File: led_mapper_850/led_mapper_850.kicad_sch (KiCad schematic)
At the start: 555 parts, among them J1 Conn_02x12_Top_Bottom

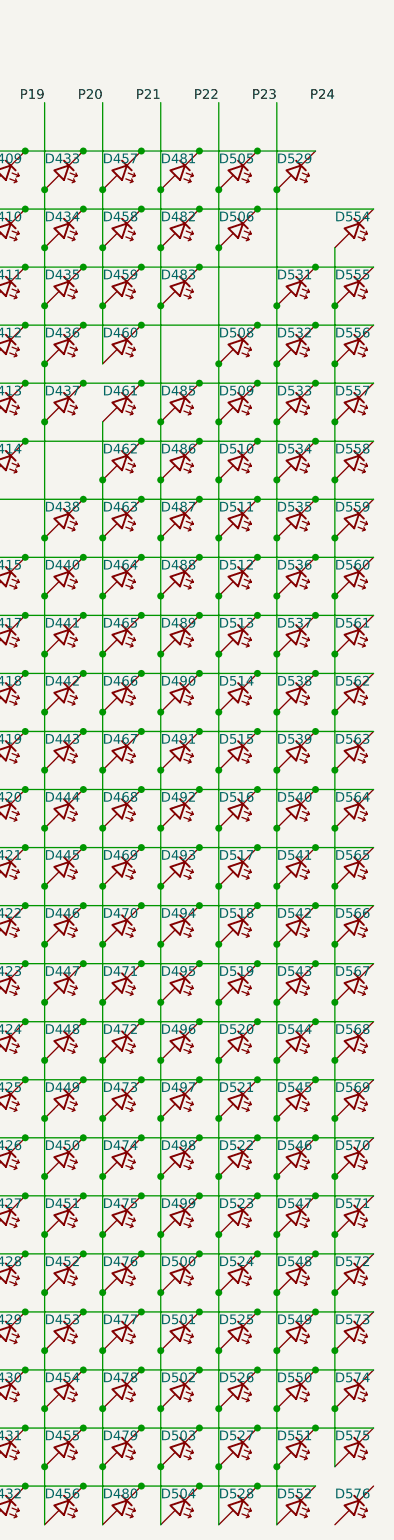
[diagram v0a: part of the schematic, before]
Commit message: run ERC & fix connections
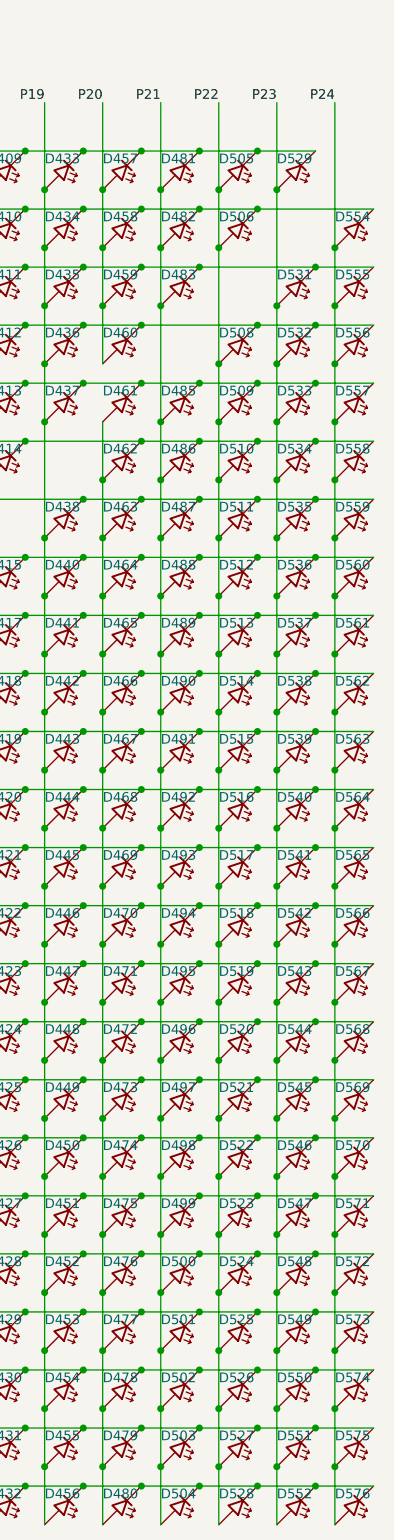
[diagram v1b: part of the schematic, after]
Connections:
- net P01: now also D576.1 (K)
- net P24: now also D554.2 (A), D555.2 (A), D556.2 (A), D557.2 (A), D558.2 (A), D559.2 (A), D560.2 (A), D561.2 (A), D562.2 (A), D563.2 (A), D564.2 (A), D565.2 (A), D566.2 (A), D567.2 (A), D568.2 (A), D569.2 (A), D570.2 (A), D571.2 (A), D572.2 (A), D573.2 (A), D574.2 (A), D575.2 (A), D576.2 (A)
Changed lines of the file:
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@@
 	)
 	(junction
+		(at 392.43 66.04)
+		(diameter 0)
+		(color 0 0 0 0)
+	)
+	(junction
 		(at 306.07 53.34)
 		(diameter 0)
@@
 	)
 	(junction
+		(at 389.89 228.6)
+		(diameter 0)
+		(color 0 0 0 0)
+	)
+	(junction
 		(at 369.57 119.38)
 		(diameter 0)
@@
 	)
 	(junction
+		(at 392.43 226.06)
+		(diameter 0)
+		(color 0 0 0 0)
+	)
+	(junction
 		(at 367.03 220.98)
 		(diameter 0)
@@
 	(wire
 		(pts
+			(xy 392.43 46.99) (xy 392.43 66.04)
+		)
+		(stroke
+			(width 0)
+			(type default)
+		)
+	)
+	(wire
+		(pts
 			(xy 260.35 106.68) (xy 267.97 106.68)
 		)
@@
 	(wire
 		(pts
+			(xy 392.43 226.06) (xy 392.43 233.68)
+		)
+		(stroke
+			(width 0)
+			(type default)
+		)
+	)
+	(wire
+		(pts
 			(xy 255.27 104.14) (xy 255.27 111.76)
 		)
@@
 		)
 		(stroke
+			(width 0)
+			(type default)
+		)
+	)
+	(wire
+		(pts
+			(xy 389.89 228.6) (xy 397.51 228.6)
+		)
+		(stroke

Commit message: associate footprints
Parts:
- D1, D10, D100, D101, D102, D103, D104, D105, D106, D107, D108, D109, D11, D110, D111, D112, D113, D114, D115, D116, D117, D118, D12, D120, D121, D122, D123, D124, D125, D126, D127, D128, D129, D13, D130, D131, D132, D133, D134, D135, D136, D137, D138, D139, D14, D140, D141, D142, D144, D145, D146, D147, D148, D149, D15, D150, D151, D152, D153, D154, D155, D156, D157, D158, D159, D16, D160, D161, D162, D163, D164, D165, D167, D168, D169, D17, D170, D171, D172, D173, D174, D175, D176, D177, D178, D179, D18, D180, D181, D182, D183, D184, D185, D186, D187, D189, D19, D190, D191, D192, D193, D194, D195, D196, D197, D198, D199, D2, D20, D200, D201, D202, D203, D204, D205, D206, D207, D208, D209, D21, D211, D212, D213, D214, D215, D216, D217, D218, D219, D22, D220, D221, D222, D223, D224, D225, D226, D227, D228, D229, D23, D230, D231, D232, D234, D235, D236, D237, D238, D239, D24, D240, D241, D242, D243, D244, D245, D246, D247, D248, D249, D25, D250, D251, D252, D253, D254, D255, D256, D258, D259, D26, D260, D261, D262, D263, D264, D265, D266, D267, D268, D269, D270, D271, D272, D273, D274, D275, D276, D277, D278, D279, D28, D280, D282, D283, D284, D285, D286, D287, D288, D289, D29, D290, D291, D292, D293, D294, D295, D296, D297, D298, D299, D3, D30, D300, D301, D302, D303, D305, D306, D307, D308, D309, D31, D310, D311, D312, D313, D314, D315, D316, D317, D318, D319, D32, D320, D321, D322, D323, D324, D325, D326, D328, D329, D33, D330, D331, D332, D333, D334, D335, D336, D337, D338, D339, D34, D340, D341, D342, D343, D344, D345, D346, D347, D348, D35, D350, D351, D352, D353, D354, D355, D356, D357, D358, D359, D36, D360, D361, D362, D363, D364, D365, D366, D367, D368, D369, D37, D370, D371, D373, D374, D375, D376, D377, D378, D379, D38, D380, D381, D382, D383, D384, D385, D386, D387, D388, D389, D39, D390, D391, D392, D393, D394, D395, D396, D397, D398, D399, D4, D40, D400, D401, D402, D403, D404, D405, D406, D407, D408, D409, D41, D410, D411, D412, D413, D414, D415, D417, D418, D419, D42, D420, D421, D422, D423, D424, D425, D426, D427, D428, D429, D43, D430, D431, D432, D433, D434, D435, D436, D437, D438, D44, D440, D441, D442, D443, D444, D445, D446, D447, D448, D449, D45, D450, D451, D452, D453, D454, D455, D456, D457, D458, D459, D46, D460, D461, D462, D463, D464, D465, D466, D467, D468, D469, D47, D470, D471, D472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: footprint (none) -> LED_SMD:LED_0201_0603Metric
- J1: footprint (none) -> ccatlib:PinSocket_2x12_P2.54mm_Vertical_SMD_custom
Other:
- moved on the sheet: D1, D10, D100, D101, D102, D103, D104, D105, D106, D107, D108, D109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

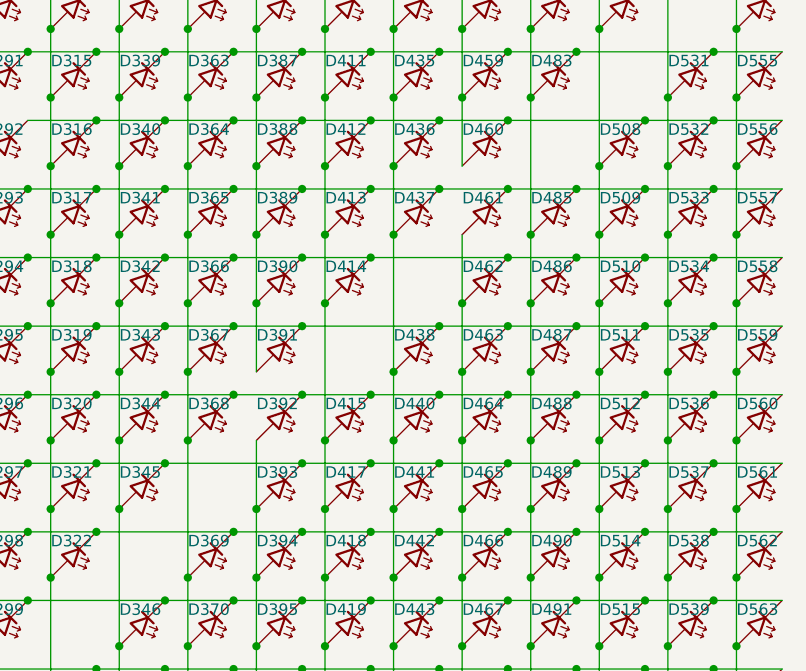
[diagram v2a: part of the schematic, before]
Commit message: fix mistakes on diagonal
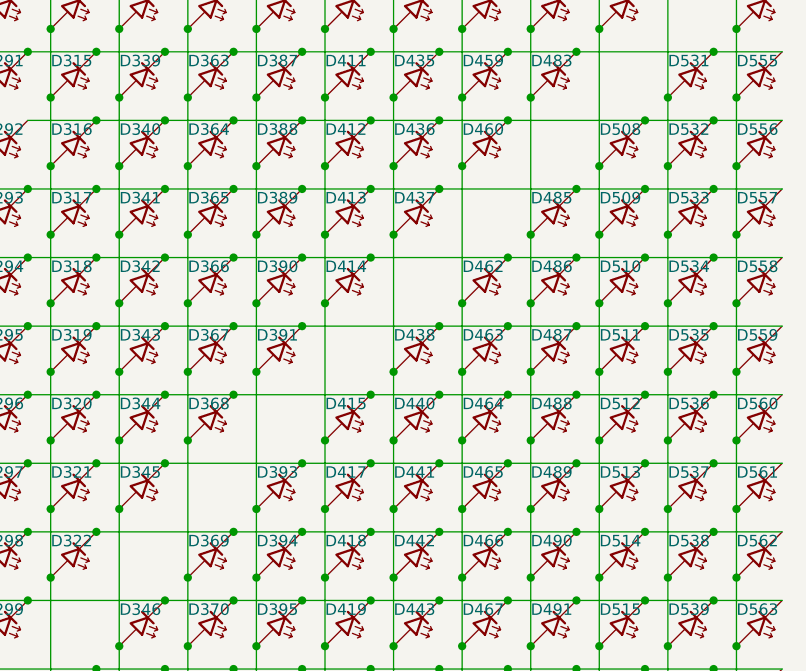
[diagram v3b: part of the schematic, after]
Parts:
- removed D392, D461: LED, LED_SMD:LED_0201_0603Metric, symbol Device:LED_45deg
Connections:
- net P17: now also D393.2 (A), D394.2 (A), D395.2 (A), D396.2 (A), D397.2 (A), D398.2 (A), D399.2 (A), D400.2 (A), D401.2 (A), D402.2 (A), D403.2 (A), D404.2 (A), D405.2 (A), D406.2 (A), D407.2 (A), D408.2 (A)
- net P20: now also D462.2 (A), D463.2 (A), D464.2 (A), D465.2 (A), D466.2 (A), D467.2 (A), D468.2 (A), D469.2 (A), D470.2 (A), D471.2 (A), D472.2 (A), D473.2 (A), D474.2 (A), D475.2 (A), D476.2 (A), D477.2 (A), D478.2 (A), D479.2 (A), D480.2 (A)
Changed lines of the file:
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@@
 	)
 	(junction
+		(at 289.56 76.2)
+		(diameter 0)
+		(color 0 0 0 0)
+	)
+	(junction
 		(at 320.04 175.26)
 		(diameter 0)
@@
 	)
 	(junction
-		(at 294.64 78.74)
-		(diameter 0)
-		(color 0 0 0 0)
-	)
-	(junction
 		(at 228.6 205.74)
 		(diameter 0)
@@
 	)
 	(junction
-		(at 271.78 101.6)
-		(diameter 0)
-		(color 0 0 0 0)
-	)
-	(junction
 		(at 213.36 106.68)
 		(diameter 0)
@@
 	)
 	(junction
+		(at 266.7 99.06)
+		(diameter 0)
+		(color 0 0 0 0)
+	)
+	(junction
 		(at 195.58 193.04)
 		(diameter 0)
@@
 	(wire
 		(pts
-			(xy 294.64 78.74) (xy 302.26 78.74)
+			(xy 287.02 78.74) (xy 302.26 78.74)
 		)
 		(stroke
@@
 	(wire
 		(pts
-			(xy 266.7 106.68) (xy 266.7 114.3)
+			(xy 266.7 99.06) (xy 266.7 114.3)
 		)
 		(stroke
@@
 	(wire
 		(pts
-			(xy 271.78 101.6) (xy 279.4 101.6)
-		)
-		(stroke
-			(width 0)
-			(type default)
-		)
-	)
-	(wire
-		(pts
 			(xy 281.94 99.06) (xy 281.94 106.68)
 		)
@@
 	(wire
 		(pts
-			(xy 264.16 101.6) (xy 271.78 101.6)
+			(xy 264.16 101.6) (xy 279.4 101.6)
 		)
 		(stroke
@@
 	(wire
 		(pts
-			(xy 287.02 78.74) (xy 294.64 78.74)
-		)
-		(stroke
-			(width 0)
-			(type default)
-		)
-	)
-	(wire
-		(pts
 			(xy 256.54 63.5) (xy 264.16 63.5)
 		)
@@
 	(wire
 		(pts
-			(xy 289.56 83.82) (xy 289.56 91.44)
+			(xy 289.56 76.2) (xy 289.56 91.44)
 		)
 		(stroke
@@
 	(symbol
 		(lib_id "Device:LED_45deg")
-		(at 292.1 81.28 90)
-		(unit 1)
-		(exclude_from_sim no)
-		(in_bom yes)
-		(on_board yes)
-		(dnp no)
-		(property "Reference" "D461"
-			(at 289.56 79.756 90)
-			(effects
-				(font
-					(size 1.27 1.27)
-				)
-				(justify right)
-			)
-		)
-		(property "Value" "LED"
-			(at 292.608 83.058 90)
-			(effects
-				(font
-					(size 1.27 1.27)
-				)
-				(justify right)
-				(hide yes)
-			)
-		)
-		(property "Footprint" "LED_SMD:LED_0201_0603Metric"
-			(at 292.1 81.28 0)
-			(effects
-				(font
-					(size 1.27 1.27)
-				)
-				(hide yes)
-			)
-		)
-		(property "Datasheet" "~"
-			(at 292.1 81.28 0)
-			(effects
-				(font
-					(size 1.27 1.27)
-				)
-				(hide yes)
-			)
-		)
-		(property "Description" "Light emitting diode, rotated by 45°"
-			(at 292.1 81.28 0)
-			(effects
-				(font
-					(size 1.27 1.27)
-				)
-				(hide yes)
-			)
-		)
-		(pin "1"
-		)
-		(pin "2"
-		)
-		(instances
-			(project "led_mapper_850"
-				(path "/51b7e780-688f-494d-9172-4437a593740a"
-					(reference "D461")
-					(unit 1)
-				)
-			)
-		)
-	)
-	(symbol
-		(lib_id "Device:LED_45deg")
 		(at 215.9 165.1 90)
 		(unit 1)
@@
 					(unit 1)
 				)
-			)
-		)
-	)
-	(symbol
-		(lib_id "Device:LED_45deg")
-		(at 269.24 104.14 90)
-		(unit 1)
-		(exclude_from_sim no)
-		(in_bom yes)
-		(on_board yes)
-		(dnp no)
-		(property "Reference" "D392"
-			(at 266.7 102.616 90)
-			(effects
-				(font
-					(size 1.27 1.27)
-				)
-				(justify right)
-			)
-		)
-		(property "Value" "LED"
-			(at 269.748 105.918 90)
-			(effects
-				(font
-					(size 1.27 1.27)
-				)
-				(justify right)
-				(hide yes)
-			)
-		)
-		(property "Footprint" "LED_SMD:LED_0201_0603Metric"
-			(at 269.24 104.14 0)
-			(effects
-				(font
-					(size 1.27 1.27)
-				)
-				(hide yes)
-			)
-		)
-		(property "Datasheet" "~"
-			(at 269.24 104.14 0)
-			(effects
-				(font
-					(size 1.27 1.27)
-				)
-				(hide yes)
-			)
-		)
-		(property "Description" "Light emitting diode, rotated by 45°"
-			(at 269.24 104.14 0)
-			(effects
-				(font
-					(size 1.27 1.27)
-				)
-				(hide yes)
-			)
-		)
-		(pin "1"
-		)
-		(pin "2"
-		)
-		(instances
-			(project "led_mapper_850"
-				(path "/51b7e780-688f-494d-9172-4437a593740a"
-					(reference "D392")
-					(unit 1)
-				)

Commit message: arrange schematic to match array geometry
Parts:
- removed D120, D144, D168, D192, D216, D240, D264, D288, D312, D336, D360, D384, D408, D432, D456, D47, D480, D504, D528, D552, D576, D71, D95: LED, LED_SMD:LED_0201_0603Metric, symbol Device:LED_45deg
- added D1000, D1001, D1002, D1003, D1004, D1005, D1006, D1007, D1008, D1009, D1010, D1011, D1012, D1013, D1014, D1015, D1016, D1017, D1018, D1019, D1020, D1021, D1022, D1023, D1024, D1025, D1026, D1027, D1028, D1029, D1030, D1031, D1032, D1033, D1034, D1035, D1036, D1037, D1038, D1039, D1040, D1041, D1042, D1043, D1044, D1045, D1046, D1047, D1048, D1049, D1050, D1051, D1052, D1053, D1054, D1055, D1056, D1057, D1058, D1059, D1060, D1061, D1062, D1063, D1064, D1065, D1066, D1067, D1068, D1069, D1070, D1071, D1072, D1073, D1074, D1075, D1076, D1077, D1078, D1079, D1080, D1081, D1082, D1083, D1084, D1085, D1086, D1087, D1088, D1089, D1090, D1091, D1092, D1093, D1094, D1095, D1096, D1097, D1098, D1099, D1100, D1101, D1102, D1103, D1104, D119, D143, D166, D188, D210, D233, D257, D27, D281, D304, D327, D349, D372, D392, D416, D439, D461, D484, D50, D507, D530, D553, D577, D578, D579, D580, D581, D582, D583, D584, D585, D586, D587, D588, D589, D590, D591, D592, D593, D594, D595, D596, D597, D598, D599, D600, D601, D602, D603, D604, D605, D606, D607, D608, D609, D610, D611, D612, D613, D614, D615, D616, D617, D618, D619, D620, D621, D622, D623, D624, D625, D626, D627, D628, D629, D630, D631, D632, D633, D634, D635, D636, D637, D638, D639, D640, D641, D642, D643, D644, D645, D646, D647, D648, D649, D650, D651, D652, D653, D654, D655, D656, D657, D658, D659, D660, D661, D662, D663, D664, D665, D666, D667, D668, D669, D670, D671, D672, D673, D674, D675, D676, D677, D678, D679, D680, D681, D682, D683, D684, D685, D686, D687, D688, D689, D690, D691, D692, D693, D694, D695, D696, D697, D698, D699, D700, D701, D702, D703, D704, D705, D706, D707, D708, D709, D710, D711, D712, D713, D714, D715, D716, D717, D718, D719, D720, D721, D722, D723, D724, D725, D726, D727, D728, D729, D730, D731, D732, D733, D734, D735, D736, D737, D738, D739, D74, D740, D741, D742, D743, D744, D745, D746, D747, D748, D749, D750, D751, D752, D753, D754, D755, D756, D757, D758, D759, D760, D761, D762, D763, D764, D765, D766, D767, D768, D769, D770, D771, D772, D773, D774, D775, D776, D777, D778, D779, D780, D781, D782, D783, D784, D785, D786, D787, D788, D789, D790, D791, D792, D793, D794, D795, D796, D797, D798, D799, D800, D801, D802, D803, D804, D805, D806, D807, D808, D809, D810, D811, D812, D813, D814, D815, D816, D817, D818, D819, D820, D821, D822, D823, D824, D825, D826, D827, D828, D829, D830, D831, D832, D833, D834, D835, D836, D837, D838, D839, D840, D841, D842, D843, D844, D845, D846, D847, D848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: LED, LED_SMD:LED_0201_0603Metric, symbol Device:LED_45deg
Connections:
- net P01: now also D1012.1 (K), D1035.1 (K), D1058.1 (K), D1081.1 (K), D1104.1 (K), D119.2 (A), D143.2 (A), D166.2 (A), D188.2 (A), D210.2 (A), D233.2 (A), D257.2 (A), D27.2 (A), D281.2 (A), D304.2 (A), D327.2 (A), D349.2 (A), D372.2 (A), D392.2 (A), D416.2 (A), D439.2 (A), D461.2 (A), D484.2 (A), D50.2 (A), D507.2 (A), D530.2 (A), D598.1 (K), D621.1 (K), D644.1 (K), D667.1 (K), D690.1 (K), D713.1 (K), D736.1 (K), D74.2 (A), D759.1 (K), D782.1 (K), D805.1 (K), D828.1 (K), D851.1 (K), D874.1 (K), D897.1 (K), D920.1 (K), D943.1 (K), D966.1 (K), D97.2 (A), D989.1 (K)
- net P02: now also D1011.1 (K), D1034.1 (K), D1057.1 (K), D1080.1 (K), D1103.1 (K), D530.1 (K), D553.2 (A), D577.2 (A), D578.2 (A), D579.2 (A), D580.2 (A), D581.2 (A), D582.2 (A), D583.2 (A), D584.2 (A), D585.2 (A), D586.2 (A), D587.2 (A), D588.2 (A), D589.2 (A), D590.2 (A), D591.2 (A), D592.2 (A), D593.2 (A), D594.2 (A), D595.2 (A), D596.2 (A), D597.2 (A), D598.2 (A), D620.1 (K), D643.1 (K), D666.1 (K), D689.1 (K), D712.1 (K), D735.1 (K), D758.1 (K), D781.1 (K), D804.1 (K), D827.1 (K), D850.1 (K), D873.1 (K), D896.1 (K), D919.1 (K), D942.1 (K), D965.1 (K), D988.1 (K); no longer D118.1 (K), D142.1 (K), D167.1 (K), D191.1 (K), D215.1 (K), D23.1 (K), D239.1 (K), D263.1 (K), D287.1 (K), D311.1 (K), D335.1 (K), D359.1 (K), D383.1 (K), D407.1 (K), D431.1 (K), D455.1 (K), D479.1 (K), D503.1 (K), D527.1 (K), D551.1 (K), D575.1 (K), D70.1 (K), D94.1 (K)
- net P03: now also D1010.1 (K), D1033.1 (K), D1056.1 (K), D1079.1 (K), D1102.1 (K), D507.1 (K), D597.1 (K), D599.2 (A), D600.2 (A), D601.2 (A), D602.2 (A), D603.2 (A), D604.2 (A), D605.2 (A), D606.2 (A), D607.2 (A), D608.2 (A), D609.2 (A), D610.2 (A), D611.2 (A), D612.2 (A), D613.2 (A), D614.2 (A), D615.2 (A), D616.2 (A), D617.2 (A), D618.2 (A), D619.2 (A), D620.2 (A), D621.2 (A), D642.1 (K), D665.1 (K), D688.1 (K), D711.1 (K), D734.1 (K), D757.1 (K), D780.1 (K), D803.1 (K), D826.1 (K), D849.1 (K), D872.1 (K), D895.1 (K), D918.1 (K), D941.1 (K), D964.1 (K), D987.1 (K); no longer D117.1 (K), D141.1 (K), D165.1 (K), D190.1 (K), D214.1 (K), D22.1 (K), D238.1 (K), D262.1 (K), D286.1 (K), D310.1 (K), D334.1 (K), D358.1 (K), D382.1 (K), D406.1 (K), D430.1 (K), D454.1 (K), D46.1 (K), D478.1 (K), D502.1 (K), D526.1 (K), D550.1 (K), D574.1 (K), D93.1 (K)
- net P04: now also D1009.1 (K), D1032.1 (K), D1055.1 (K), D1078.1 (K), D1101.1 (K), D484.1 (K), D596.1 (K), D619.1 (K), D622.2 (A), D623.2 (A), D624.2 (A), D625.2 (A), D626.2 (A), D627.2 (A), D628.2 (A), D629.2 (A), D630.2 (A), D631.2 (A), D632.2 (A), D633.2 (A), D634.2 (A), D635.2 (A), D636.2 (A), D637.2 (A), D638.2 (A), D639.2 (A), D640.2 (A), D641.2 (A), D642.2 (A), D643.2 (A), D644.2 (A), D664.1 (K), D687.1 (K), D710.1 (K), D733.1 (K), D756.1 (K), D779.1 (K), D802.1 (K), D825.1 (K), D848.1 (K), D871.1 (K), D894.1 (K), D917.1 (K), D940.1 (K), D963.1 (K), D986.1 (K); no longer D116.1 (K), D140.1 (K), D164.1 (K), D189.1 (K), D21.1 (K), D213.1 (K), D237.1 (K), D261.1 (K), D285.1 (K), D309.1 (K), D333.1 (K), D357.1 (K), D381.1 (K), D405.1 (K), D429.1 (K), D45.1 (K), D453.1 (K), D477.1 (K), D501.1 (K), D525.1 (K), D549.1 (K), D573.1 (K), D69.1 (K)
- net P05: now also D1008.1 (K), D1031.1 (K), D1054.1 (K), D1077.1 (K), D1100.1 (K), D461.1 (K), D595.1 (K), D618.1 (K), D641.1 (K), D645.2 (A), D646.2 (A), D647.2 (A), D648.2 (A), D649.2 (A), D650.2 (A), D651.2 (A), D652.2 (A), D653.2 (A), D654.2 (A), D655.2 (A), D656.2 (A), D657.2 (A), D658.2 (A), D659.2 (A), D660.2 (A), D661.2 (A), D662.2 (A), D663.2 (A), D664.2 (A), D665.2 (A), D666.2 (A), D667.2 (A), D686.1 (K), D709.1 (K), D732.1 (K), D755.1 (K), D778.1 (K), D801.1 (K), D824.1 (K), D847.1 (K), D870.1 (K), D893.1 (K), D916.1 (K), D939.1 (K), D962.1 (K), D985.1 (K); no longer D139.1 (K), D163.1 (K), D187.1 (K), D20.1 (K), D212.1 (K), D236.1 (K), D260.1 (K), D284.1 (K), D308.1 (K), D332.1 (K), D356.1 (K), D380.1 (K), D404.1 (K), D428.1 (K), D44.1 (K), D452.1 (K), D476.1 (K), D500.1 (K), D524.1 (K), D548.1 (K), D572.1 (K), D68.1 (K), D92.1 (K)
- net P06: now also D1007.1 (K), D1030.1 (K), D1053.1 (K), D1076.1 (K), D1099.1 (K), D439.1 (K), D594.1 (K), D617.1 (K), D640.1 (K), D663.1 (K), D668.2 (A), D669.2 (A), D670.2 (A), D671.2 (A), D672.2 (A), D673.2 (A), D674.2 (A), D675.2 (A), D676.2 (A), D677.2 (A), D678.2 (A), D679.2 (A), D680.2 (A), D681.2 (A), D682.2 (A), D683.2 (A), D684.2 (A), D685.2 (A), D686.2 (A), D687.2 (A), D688.2 (A), D689.2 (A), D690.2 (A), D708.1 (K), D731.1 (K), D754.1 (K), D777.1 (K), D800.1 (K), D823.1 (K), D846.1 (K), D869.1 (K), D892.1 (K), D915.1 (K), D938.1 (K), D961.1 (K), D984.1 (K); no longer D115.1 (K), D162.1 (K), D186.1 (K), D19.1 (K), D211.1 (K), D235.1 (K), D259.1 (K), D283.1 (K), D307.1 (K), D331.1 (K), D355.1 (K), D379.1 (K), D403.1 (K), D427.1 (K), D43.1 (K), D451.1 (K), D475.1 (K), D499.1 (K), D523.1 (K), D547.1 (K), D571.1 (K), D67.1 (K), D91.1 (K)
- net P07: now also D1006.1 (K), D1029.1 (K), D1052.1 (K), D1075.1 (K), D1098.1 (K), D416.1 (K), D593.1 (K), D616.1 (K), D639.1 (K), D662.1 (K), D685.1 (K), D691.2 (A), D692.2 (A), D693.2 (A), D694.2 (A), D695.2 (A), D696.2 (A), D697.2 (A), D698.2 (A), D699.2 (A), D700.2 (A), D701.2 (A), D702.2 (A), D703.2 (A), D704.2 (A), D705.2 (A), D706.2 (A), D707.2 (A), D708.2 (A), D709.2 (A), D710.2 (A), D711.2 (A), D712.2 (A), D713.2 (A), D730.1 (K), D753.1 (K), D776.1 (K), D799.1 (K), D822.1 (K), D845.1 (K), D868.1 (K), D891.1 (K), D914.1 (K), D937.1 (K), D960.1 (K), D983.1 (K); no longer D114.1 (K), D138.1 (K), D18.1 (K), D185.1 (K), D209.1 (K), D234.1 (K), D258.1 (K), D282.1 (K), D306.1 (K), D330.1 (K), D354.1 (K), D378.1 (K), D402.1 (K), D42.1 (K), D426.1 (K), D450.1 (K), D474.1 (K), D498.1 (K), D522.1 (K), D546.1 (K), D570.1 (K), D66.1 (K), D90.1 (K)
- net P08: now also D1005.1 (K), D1028.1 (K), D1051.1 (K), D1074.1 (K), D1097.1 (K), D392.1 (K), D592.1 (K), D615.1 (K), D638.1 (K), D661.1 (K), D684.1 (K), D707.1 (K), D714.2 (A), D715.2 (A), D716.2 (A), D717.2 (A), D718.2 (A), D719.2 (A), D720.2 (A), D721.2 (A), D722.2 (A), D723.2 (A), D724.2 (A), D725.2 (A), D726.2 (A), D727.2 (A), D728.2 (A), D729.2 (A), D730.2 (A), D731.2 (A), D732.2 (A), D733.2 (A), D734.2 (A), D735.2 (A), D736.2 (A), D752.1 (K), D775.1 (K), D798.1 (K), D821.1 (K), D844.1 (K), D867.1 (K), D890.1 (K), D913.1 (K), D936.1 (K), D959.1 (K), D982.1 (K); no longer D113.1 (K), D137.1 (K), D161.1 (K), D17.1 (K), D208.1 (K), D232.1 (K), D256.1 (K), D280.1 (K), D305.1 (K), D329.1 (K), D353.1 (K), D377.1 (K), D401.1 (K), D41.1 (K), D425.1 (K), D449.1 (K), D473.1 (K), D497.1 (K), D521.1 (K), D545.1 (K), D569.1 (K), D65.1 (K), D89.1 (K)
- net P09: now also D1004.1 (K), D1027.1 (K), D1050.1 (K), D1073.1 (K), D1096.1 (K), D372.1 (K), D591.1 (K), D614.1 (K), D637.1 (K), D660.1 (K), D683.1 (K), D706.1 (K), D729.1 (K), D737.2 (A), D738.2 (A), D739.2 (A), D740.2 (A), D741.2 (A), D742.2 (A), D743.2 (A), D744.2 (A), D745.2 (A), D746.2 (A), D747.2 (A), D748.2 (A), D749.2 (A), D750.2 (A), D751.2 (A), D752.2 (A), D753.2 (A), D754.2 (A), D755.2 (A), D756.2 (A), D757.2 (A), D758.2 (A), D759.2 (A), D774.1 (K), D797.1 (K), D820.1 (K), D843.1 (K), D866.1 (K), D889.1 (K), D912.1 (K), D935.1 (K), D958.1 (K), D981.1 (K); no longer D112.1 (K), D136.1 (K), D16.1 (K), D160.1 (K), D184.1 (K), D231.1 (K), D255.1 (K), D279.1 (K), D303.1 (K), D328.1 (K), D352.1 (K), D376.1 (K), D40.1 (K), D400.1 (K), D424.1 (K), D448.1 (K), D472.1 (K), D496.1 (K), D520.1 (K), D544.1 (K), D568.1 (K), D64.1 (K), D88.1 (K)
- net P10: now also D1003.1 (K), D1026.1 (K), D1049.1 (K), D1072.1 (K), D1095.1 (K), D349.1 (K), D590.1 (K), D613.1 (K), D636.1 (K), D659.1 (K), D682.1 (K), D705.1 (K), D728.1 (K), D751.1 (K), D760.2 (A), D761.2 (A), D762.2 (A), D763.2 (A), D764.2 (A), D765.2 (A), D766.2 (A), D767.2 (A), D768.2 (A), D769.2 (A), D770.2 (A), D771.2 (A), D772.2 (A), D773.2 (A), D774.2 (A), D775.2 (A), D776.2 (A), D777.2 (A), D778.2 (A), D779.2 (A), D780.2 (A), D781.2 (A), D782.2 (A), D796.1 (K), D819.1 (K), D842.1 (K), D865.1 (K), D888.1 (K), D911.1 (K), D934.1 (K), D957.1 (K), D980.1 (K); no longer D111.1 (K), D135.1 (K), D15.1 (K), D159.1 (K), D183.1 (K), D207.1 (K), D254.1 (K), D278.1 (K), D302.1 (K), D326.1 (K), D351.1 (K), D375.1 (K), D39.1 (K), D399.1 (K), D423.1 (K), D447.1 (K), D471.1 (K), D495.1 (K), D519.1 (K), D543.1 (K), D567.1 (K), D63.1 (K), D87.1 (K)
- net P11: now also D1002.1 (K), D1025.1 (K), D1048.1 (K), D1071.1 (K), D1094.1 (K), D327.1 (K), D589.1 (K), D612.1 (K), D635.1 (K), D658.1 (K), D681.1 (K), D704.1 (K), D727.1 (K), D750.1 (K), D773.1 (K), D783.2 (A), D784.2 (A), D785.2 (A), D786.2 (A), D787.2 (A), D788.2 (A), D789.2 (A), D790.2 (A), D791.2 (A), D792.2 (A), D793.2 (A), D794.2 (A), D795.2 (A), D796.2 (A), D797.2 (A), D798.2 (A), D799.2 (A), D800.2 (A), D801.2 (A), D802.2 (A), D803.2 (A), D804.2 (A), D805.2 (A), D818.1 (K), D841.1 (K), D864.1 (K), D887.1 (K), D910.1 (K), D933.1 (K), D956.1 (K), D979.1 (K); no longer D110.1 (K), D134.1 (K), D14.1 (K), D158.1 (K), D182.1 (K), D206.1 (K), D230.1 (K), D277.1 (K), D301.1 (K), D325.1 (K), D350.1 (K), D374.1 (K), D38.1 (K), D398.1 (K), D422.1 (K), D446.1 (K), D470.1 (K), D494.1 (K), D518.1 (K), D542.1 (K), D566.1 (K), D62.1 (K), D86.1 (K)
- net P12: now also D1001.1 (K), D1024.1 (K), D1047.1 (K), D1070.1 (K), D1093.1 (K), D304.1 (K), D588.1 (K), D611.1 (K), D634.1 (K), D657.1 (K), D680.1 (K), D703.1 (K), D726.1 (K), D749.1 (K), D772.1 (K), D795.1 (K), D806.2 (A), D807.2 (A), D808.2 (A), D809.2 (A), D810.2 (A), D811.2 (A), D812.2 (A), D813.2 (A), D814.2 (A), D815.2 (A), D816.2 (A), D817.2 (A), D818.2 (A), D819.2 (A), D820.2 (A), D821.2 (A), D822.2 (A), D823.2 (A), D824.2 (A), D825.2 (A), D826.2 (A), D827.2 (A), D828.2 (A), D840.1 (K), D863.1 (K), D886.1 (K), D909.1 (K), D932.1 (K), D955.1 (K), D978.1 (K); no longer D109.1 (K), D13.1 (K), D133.1 (K), D157.1 (K), D181.1 (K), D205.1 (K), D229.1 (K), D253.1 (K), D277.2 (A), D278.2 (A), D279.2 (A), D280.2 (A), D282.2 (A), D283.2 (A), D284.2 (A), D285.2 (A), D286.2 (A), D287.2 (A), D300.1 (K), D324.1 (K), D348.1 (K), D37.1 (K), D373.1 (K), D397.1 (K), D421.1 (K), D445.1 (K), D469.1 (K), D493.1 (K), D517.1 (K), D541.1 (K), D565.1 (K), D61.1 (K), D85.1 (K)
- net P13: now also D1000.1 (K), D1023.1 (K), D1046.1 (K), D1069.1 (K), D1092.1 (K), D281.1 (K), D587.1 (K), D610.1 (K), D633.1 (K), D656.1 (K), D679.1 (K), D702.1 (K), D725.1 (K), D748.1 (K), D771.1 (K), D794.1 (K), D817.1 (K), D829.2 (A), D830.2 (A), D831.2 (A), D832.2 (A), D833.2 (A), D834.2 (A), D835.2 (A), D836.2 (A), D837.2 (A), D838.2 (A), D839.2 (A), D840.2 (A), D841.2 (A), D842.2 (A), D843.2 (A), D844.2 (A), D845.2 (A), D846.2 (A), D847.2 (A), D848.2 (A), D849.2 (A), D850.2 (A), D851.2 (A), D862.1 (K), D885.1 (K), D908.1 (K), D931.1 (K), D954.1 (K), D977.1 (K)
- net P14: now also D118.1 (K), D142.1 (K), D167.1 (K), D191.1 (K), D215.1 (K), D23.1 (K), D239.1 (K), D263.1 (K), D287.1 (K), D311.1 (K), D335.1 (K), D359.1 (K), D383.1 (K), D407.1 (K), D431.1 (K), D455.1 (K), D479.1 (K), D503.1 (K), D527.1 (K), D551.1 (K), D575.1 (K), D70.1 (K), D94.1 (K), D1022.1 (K), D1045.1 (K), D1068.1 (K), D1091.1 (K), D257.1 (K), D586.1 (K), D609.1 (K), D632.1 (K), D655.1 (K), D678.1 (K), D701.1 (K), D724.1 (K), D747.1 (K), D770.1 (K), D793.1 (K), D816.1 (K), D839.1 (K), D852.2 (A), D853.2 (A), D854.2 (A), D855.2 (A), D856.2 (A), D857.2 (A), D858.2 (A), D859.2 (A), D860.2 (A), D861.2 (A), D862.2 (A), D863.2 (A), D864.2 (A), D865.2 (A), D866.2 (A), D867.2 (A), D868.2 (A), D869.2 (A), D870.2 (A), D871.2 (A), D872.2 (A), D873.2 (A), D874.2 (A), D884.1 (K), D907.1 (K), D930.1 (K), D953.1 (K), D976.1 (K), D999.1 (K)
- net P15: now also D117.1 (K), D141.1 (K), D165.1 (K), D190.1 (K), D214.1 (K), D22.1 (K), D238.1 (K), D262.1 (K), D286.1 (K), D310.1 (K), D334.1 (K), D358.1 (K), D382.1 (K), D406.1 (K), D430.1 (K), D454.1 (K), D46.1 (K), D478.1 (K), D502.1 (K), D526.1 (K), D550.1 (K), D574.1 (K), D93.1 (K), D1021.1 (K), D1044.1 (K), D1067.1 (K), D1090.1 (K), D233.1 (K), D585.1 (K), D608.1 (K), D631.1 (K), D654.1 (K), D677.1 (K), D700.1 (K), D723.1 (K), D746.1 (K), D769.1 (K), D792.1 (K), D815.1 (K), D838.1 (K), D861.1 (K), D875.2 (A), D876.2 (A), D877.2 (A), D878.2 (A), D879.2 (A), D880.2 (A), D881.2 (A), D882.2 (A), D883.2 (A), D884.2 (A), D885.2 (A), D886.2 (A), D887.2 (A), D888.2 (A), D889.2 (A), D890.2 (A), D891.2 (A), D892.2 (A), D893.2 (A), D894.2 (A), D895.2 (A), D896.2 (A), D897.2 (A), D906.1 (K), D929.1 (K), D952.1 (K), D975.1 (K), D998.1 (K)
- net P16: now also D116.1 (K), D140.1 (K), D164.1 (K), D189.1 (K), D21.1 (K), D213.1 (K), D237.1 (K), D261.1 (K), D285.1 (K), D309.1 (K), D333.1 (K), D357.1 (K), D381.1 (K), D405.1 (K), D429.1 (K), D45.1 (K), D453.1 (K), D477.1 (K), D501.1 (K), D525.1 (K), D549.1 (K), D573.1 (K), D69.1 (K), D1020.1 (K), D1043.1 (K), D1066.1 (K), D1089.1 (K), D210.1 (K), D584.1 (K), D607.1 (K), D630.1 (K), D653.1 (K), D676.1 (K), D699.1 (K), D722.1 (K), D745.1 (K), D768.1 (K), D791.1 (K), D814.1 (K), D837.1 (K), D860.1 (K), D883.1 (K), D898.2 (A), D899.2 (A), D900.2 (A), D901.2 (A), D902.2 (A), D903.2 (A), D904.2 (A), D905.2 (A), D906.2 (A), D907.2 (A), D908.2 (A), D909.2 (A), D910.2 (A), D911.2 (A), D912.2 (A), D913.2 (A), D914.2 (A), D915.2 (A), D916.2 (A), D917.2 (A), D918.2 (A), D919.2 (A), D920.2 (A), D928.1 (K), D951.1 (K), D974.1 (K), D997.1 (K)
- net P17: now also D139.1 (K), D163.1 (K), D187.1 (K), D20.1 (K), D212.1 (K), D236.1 (K), D260.1 (K), D284.1 (K), D308.1 (K), D332.1 (K), D356.1 (K), D380.1 (K), D404.1 (K), D428.1 (K), D44.1 (K), D452.1 (K), D476.1 (K), D500.1 (K), D524.1 (K), D548.1 (K), D572.1 (K), D68.1 (K), D92.1 (K), D1019.1 (K), D1042.1 (K), D1065.1 (K), D1088.1 (K), D188.1 (K), D583.1 (K), D606.1 (K), D629.1 (K), D652.1 (K), D675.1 (K), D698.1 (K), D721.1 (K), D744.1 (K), D767.1 (K), D790.1 (K), D813.1 (K), D836.1 (K), D859.1 (K), D882.1 (K), D905.1 (K), D921.2 (A), D922.2 (A), D923.2 (A), D924.2 (A), D925.2 (A), D926.2 (A), D927.2 (A), D928.2 (A), D929.2 (A), D930.2 (A), D931.2 (A), D932.2 (A), D933.2 (A), D934.2 (A), D935.2 (A), D936.2 (A), D937.2 (A), D938.2 (A), D939.2 (A), D940.2 (A), D941.2 (A), D942.2 (A), D943.2 (A), D950.1 (K), D973.1 (K), D996.1 (K)
- net P18: now also D115.1 (K), D162.1 (K), D186.1 (K), D19.1 (K), D211.1 (K), D235.1 (K), D259.1 (K), D283.1 (K), D307.1 (K), D331.1 (K), D355.1 (K), D379.1 (K), D403.1 (K), D427.1 (K), D43.1 (K), D451.1 (K), D475.1 (K), D499.1 (K), D523.1 (K), D547.1 (K), D571.1 (K), D67.1 (K), D91.1 (K), D1018.1 (K), D1041.1 (K), D1064.1 (K), D1087.1 (K), D166.1 (K), D582.1 (K), D605.1 (K), D628.1 (K), D651.1 (K), D674.1 (K), D697.1 (K), D720.1 (K), D743.1 (K), D766.1 (K), D789.1 (K), D812.1 (K), D835.1 (K), D858.1 (K), D881.1 (K), D904.1 (K), D927.1 (K), D944.2 (A), D945.2 (A), D946.2 (A), D947.2 (A), D948.2 (A), D949.2 (A), D950.2 (A), D951.2 (A), D952.2 (A), D953.2 (A), D954.2 (A), D955.2 (A), D956.2 (A), D957.2 (A), D958.2 (A), D959.2 (A), D960.2 (A), D961.2 (A), D962.2 (A), D963.2 (A), D964.2 (A), D965.2 (A), D966.2 (A), D972.1 (K), D995.1 (K)
- net P19: now also D114.1 (K), D138.1 (K), D18.1 (K), D185.1 (K), D209.1 (K), D234.1 (K), D258.1 (K), D282.1 (K), D306.1 (K), D330.1 (K), D354.1 (K), D378.1 (K), D402.1 (K), D42.1 (K), D426.1 (K), D450.1 (K), D474.1 (K), D498.1 (K), D522.1 (K), D546.1 (K), D570.1 (K), D66.1 (K), D90.1 (K), D1017.1 (K), D1040.1 (K), D1063.1 (K), D1086.1 (K), D143.1 (K), D581.1 (K), D604.1 (K), D627.1 (K), D650.1 (K), D673.1 (K), D696.1 (K), D719.1 (K), D742.1 (K), D765.1 (K), D788.1 (K), D811.1 (K), D834.1 (K), D857.1 (K), D880.1 (K), D903.1 (K), D926.1 (K), D949.1 (K), D967.2 (A), D968.2 (A), D969.2 (A), D970.2 (A), D971.2 (A), D972.2 (A), D973.2 (A), D974.2 (A), D975.2 (A), D976.2 (A), D977.2 (A), D978.2 (A), D979.2 (A), D980.2 (A), D981.2 (A), D982.2 (A), D983.2 (A), D984.2 (A), D985.2 (A), D986.2 (A), D987.2 (A), D988.2 (A), D989.2 (A), D994.1 (K)
- net P20: now also D113.1 (K), D137.1 (K), D161.1 (K), D17.1 (K), D208.1 (K), D232.1 (K), D256.1 (K), D280.1 (K), D305.1 (K), D329.1 (K), D353.1 (K), D377.1 (K), D401.1 (K), D41.1 (K), D425.1 (K), D449.1 (K), D473.1 (K), D497.1 (K), D521.1 (K), D545.1 (K), D569.1 (K), D65.1 (K), D89.1 (K), D1000.2 (A), D1001.2 (A), D1002.2 (A), D1003.2 (A), D1004.2 (A), D1005.2 (A), D1006.2 (A), D1007.2 (A), D1008.2 (A), D1009.2 (A), D1010.2 (A), D1011.2 (A), D1012.2 (A), D1016.1 (K), D1039.1 (K), D1062.1 (K), D1085.1 (K), D119.1 (K), D580.1 (K), D603.1 (K), D626.1 (K), D649.1 (K), D672.1 (K), D695.1 (K), D718.1 (K), D741.1 (K), D764.1 (K), D787.1 (K), D810.1 (K), D833.1 (K), D856.1 (K), D879.1 (K), D902.1 (K), D925.1 (K), D948.1 (K), D971.1 (K), D990.2 (A), D991.2 (A), D992.2 (A), D993.2 (A), D994.2 (A), D995.2 (A), D996.2 (A), D997.2 (A), D998.2 (A), D999.2 (A)
- net P21: now also D1013.2 (A), D1014.2 (A), D1015.2 (A), D1016.2 (A), D1017.2 (A), D1018.2 (A), D1019.2 (A), D1020.2 (A), D1021.2 (A), D1022.2 (A), D1023.2 (A), D1024.2 (A), D1025.2 (A), D1026.2 (A), D1027.2 (A), D1028.2 (A), D1029.2 (A), D1030.2 (A), D1031.2 (A), D1032.2 (A), D1033.2 (A), D1034.2 (A), D1035.2 (A), D579.1 (K), D602.1 (K), D625.1 (K), D648.1 (K), D671.1 (K), D694.1 (K), D717.1 (K), D740.1 (K), D763.1 (K), D786.1 (K), D809.1 (K), D97.1 (K)
- net P22: now also D111.1 (K), D135.1 (K), D15.1 (K), D159.1 (K), D183.1 (K), D207.1 (K), D254.1 (K), D278.1 (K), D302.1 (K), D326.1 (K), D351.1 (K), D375.1 (K), D39.1 (K), D399.1 (K), D423.1 (K), D447.1 (K), D471.1 (K), D495.1 (K), D519.1 (K), D543.1 (K), D567.1 (K), D63.1 (K), D87.1 (K), D1015.1 (K), D1036.2 (A), D1037.2 (A), D1038.2 (A), D1039.2 (A), D1040.2 (A), D1041.2 (A), D1042.2 (A), D1043.2 (A), D1044.2 (A), D1045.2 (A), D1046.2 (A), D1047.2 (A), D1048.2 (A), D1049.2 (A), D1050.2 (A), D1051.2 (A), D1052.2 (A), D1053.2 (A), D1054.2 (A), D1055.2 (A), D1056.2 (A), D1057.2 (A), D1058.2 (A), D1060.1 (K), D1083.1 (K), D578.1 (K), D601.1 (K), D624.1 (K), D647.1 (K), D670.1 (K), D693.1 (K), D716.1 (K), D739.1 (K), D74.1 (K), D762.1 (K), D785.1 (K), D808.1 (K), D831.1 (K), D854.1 (K), D877.1 (K), D900.1 (K), D923.1 (K), D946.1 (K), D969.1 (K), D992.1 (K)
- net P23: now also D110.1 (K), D134.1 (K), D14.1 (K), D158.1 (K), D182.1 (K), D206.1 (K), D230.1 (K), D277.1 (K), D301.1 (K), D325.1 (K), D350.1 (K), D374.1 (K), D38.1 (K), D398.1 (K), D422.1 (K), D446.1 (K), D470.1 (K), D494.1 (K), D518.1 (K), D542.1 (K), D566.1 (K), D62.1 (K), D86.1 (K), D1014.1 (K), D1037.1 (K), D1059.2 (A), D1060.2 (A), D1061.2 (A), D1062.2 (A), D1063.2 (A), D1064.2 (A), D1065.2 (A), D1066.2 (A), D1067.2 (A), D1068.2 (A), D1069.2 (A), D1070.2 (A), D1071.2 (A), D1072.2 (A), D1073.2 (A), D1074.2 (A), D1075.2 (A), D1076.2 (A), D1077.2 (A), D1078.2 (A), D1079.2 (A), D1080.2 (A), D1081.2 (A), D1082.1 (K), D50.1 (K), D577.1 (K), D600.1 (K), D623.1 (K), D646.1 (K), D669.1 (K), D692.1 (K), D715.1 (K), D738.1 (K), D761.1 (K), D784.1 (K), D807.1 (K), D830.1 (K), D853.1 (K), D876.1 (K), D899.1 (K), D922.1 (K), D945.1 (K), D968.1 (K), D991.1 (K)
- net P24: now also D109.1 (K), D13.1 (K), D133.1 (K), D157.1 (K), D181.1 (K), D205.1 (K), D229.1 (K), D253.1 (K), D300.1 (K), D324.1 (K), D348.1 (K), D37.1 (K), D373.1 (K), D397.1 (K), D421.1 (K), D445.1 (K), D469.1 (K), D493.1 (K), D517.1 (K), D541.1 (K), D565.1 (K), D61.1 (K), D85.1 (K), D1013.1 (K), D1036.1 (K), D1059.1 (K), D1082.2 (A), D1083.2 (A), D1084.2 (A), D1085.2 (A), D1086.2 (A), D1087.2 (A), D1088.2 (A), D1089.2 (A), D1090.2 (A), D1091.2 (A), D1092.2 (A), D1093.2 (A), D1094.2 (A), D1095.2 (A), D1096.2 (A), D1097.2 (A), D1098.2 (A), D1099.2 (A), D1100.2 (A), D1101.2 (A), D1102.2 (A), D1103.2 (A), D1104.2 (A), D27.1 (K), D553.1 (K), D599.1 (K), D622.1 (K), D645.1 (K), D668.1 (K), D691.1 (K), D714.1 (K), D737.1 (K), D760.1 (K), D783.1 (K), D806.1 (K), D829.1 (K), D852.1 (K), D875.1 (K), D898.1 (K), D921.1 (K), D944.1 (K), D967.1 (K), D990.1 (K)
- net at D292.1 (K), D316.1 (K), D340.1 (K)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: now also D112.1 (K), D136.1 (K), D16.1 (K), D160.1 (K), D184.1 (K), D231.1 (K), D255.1 (K), D279.1 (K), D303.1 (K), D328.1 (K), D352.1 (K), D376.1 (K), D40.1 (K), D400.1 (K), D424.1 (K), D448.1 (K), D472.1 (K), D496.1 (K), D520.1 (K), D544.1 (K), D568.1 (K), D64.1 (K), D88.1 (K)
- new net: D277.2 (A), D278.2 (A), D279.2 (A), D280.2 (A), D282.2 (A), D283.2 (A), D284.2 (A), D285.2 (A), D286.2 (A), D287.2 (A)
- new net: D1038.1 (K), D1061.1 (K), D1084.1 (K), D832.1 (K), D855.1 (K), D878.1 (K), D901.1 (K), D924.1 (K), D947.1 (K), D970.1 (K), D993.1 (K)
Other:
- moved on the sheet: D1, D10, D100, D101, D102, D103, D104, D105, D106, D107, D108, D109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
